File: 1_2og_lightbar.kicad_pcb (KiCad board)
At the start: 2 copper layers, 61.7 x 18.6 mm, 35 parts, among them J1 Conn_01x03

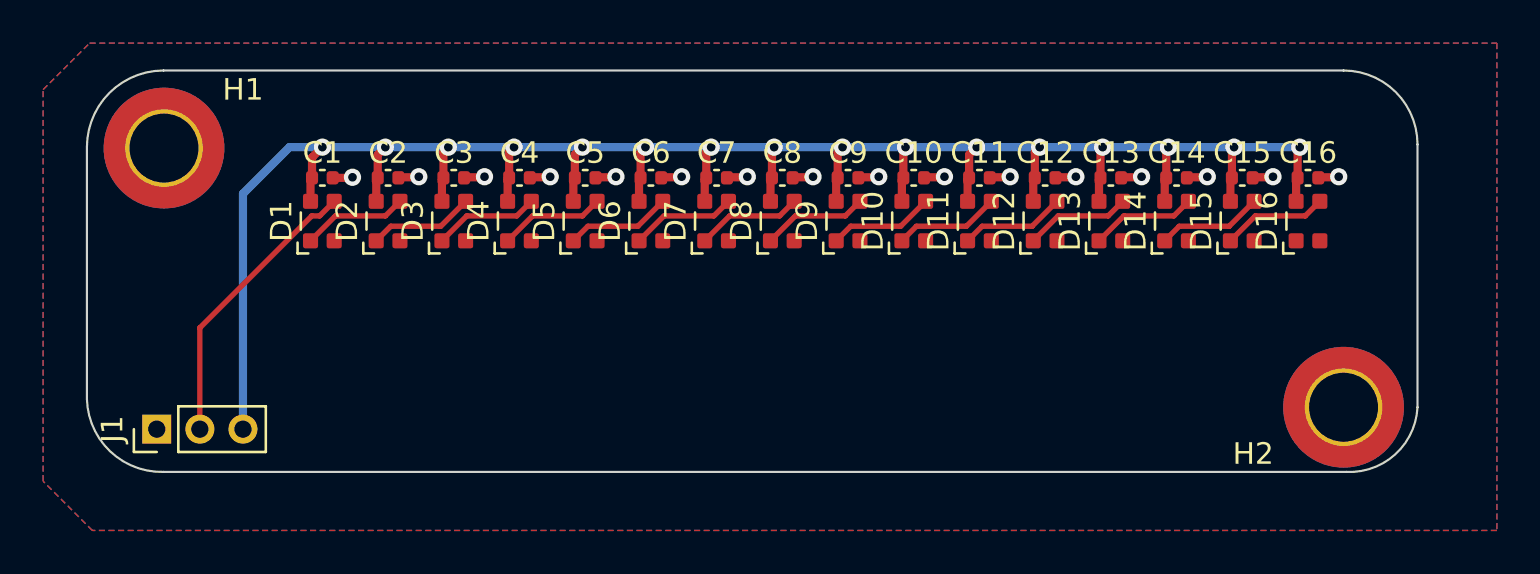
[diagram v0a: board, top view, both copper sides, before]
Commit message: add lightbar kinda (gerbers have not been fully updated yet, bom is broken)
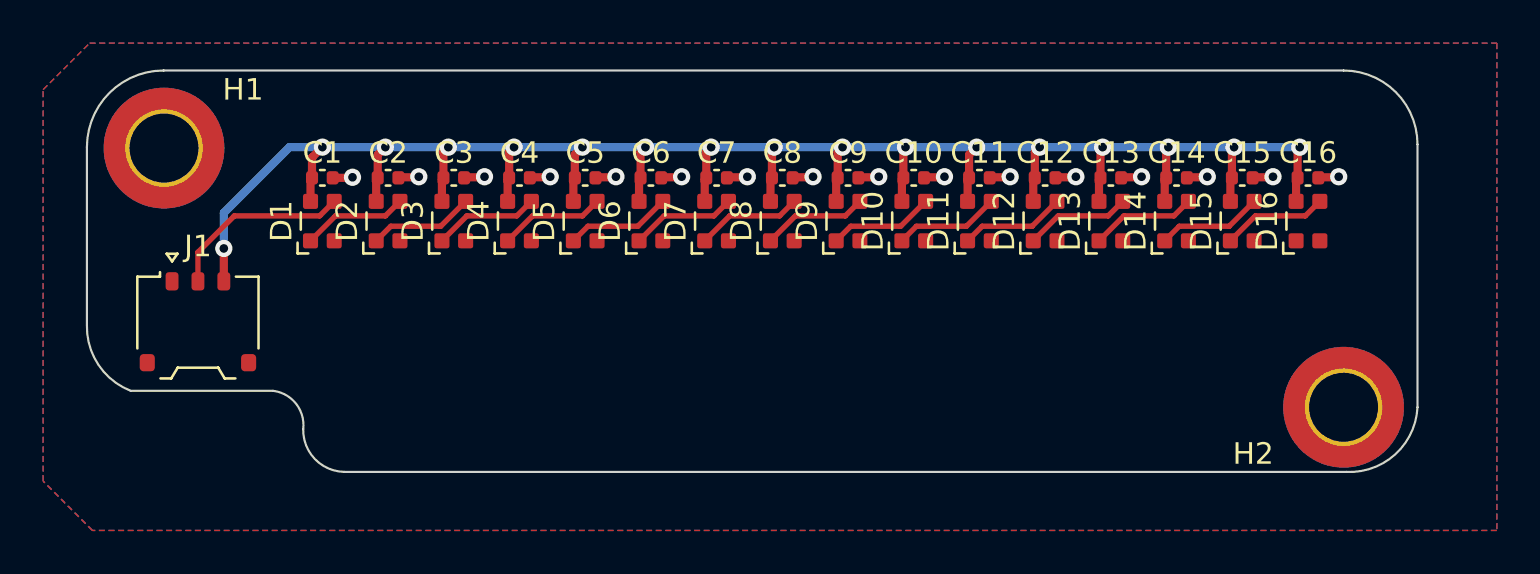
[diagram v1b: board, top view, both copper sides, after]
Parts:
- J1: footprint Connector_PinHeader_2.00mm:PinHeader_1x03_P2.00mm_Vertical -> Connector_Molex:Molex_Pico-EZmate_78171-0003_1x03-1MP_P1.20mm_Vertical
- moved J1 5.34 mm to (24.5, 28.4), turned to 0 degrees
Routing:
- net +5V: track 103.0 -> 96.5 mm, vias 16 -> 17
- net LIGHTBAR_RGB_OUT: track 13.4 -> 8.65 mm
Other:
- outline, holes or cut-outs redrawn
